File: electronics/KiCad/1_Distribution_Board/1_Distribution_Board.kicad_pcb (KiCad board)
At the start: 2 copper layers, 10 parts, among them J1 Conn_01x02, J2 Conn_01x04, J5 Conn_01x04, J6 Conn_01x10, J7 Conn_01x02, J8 Barrel_Jack, J9 Conn_01x02

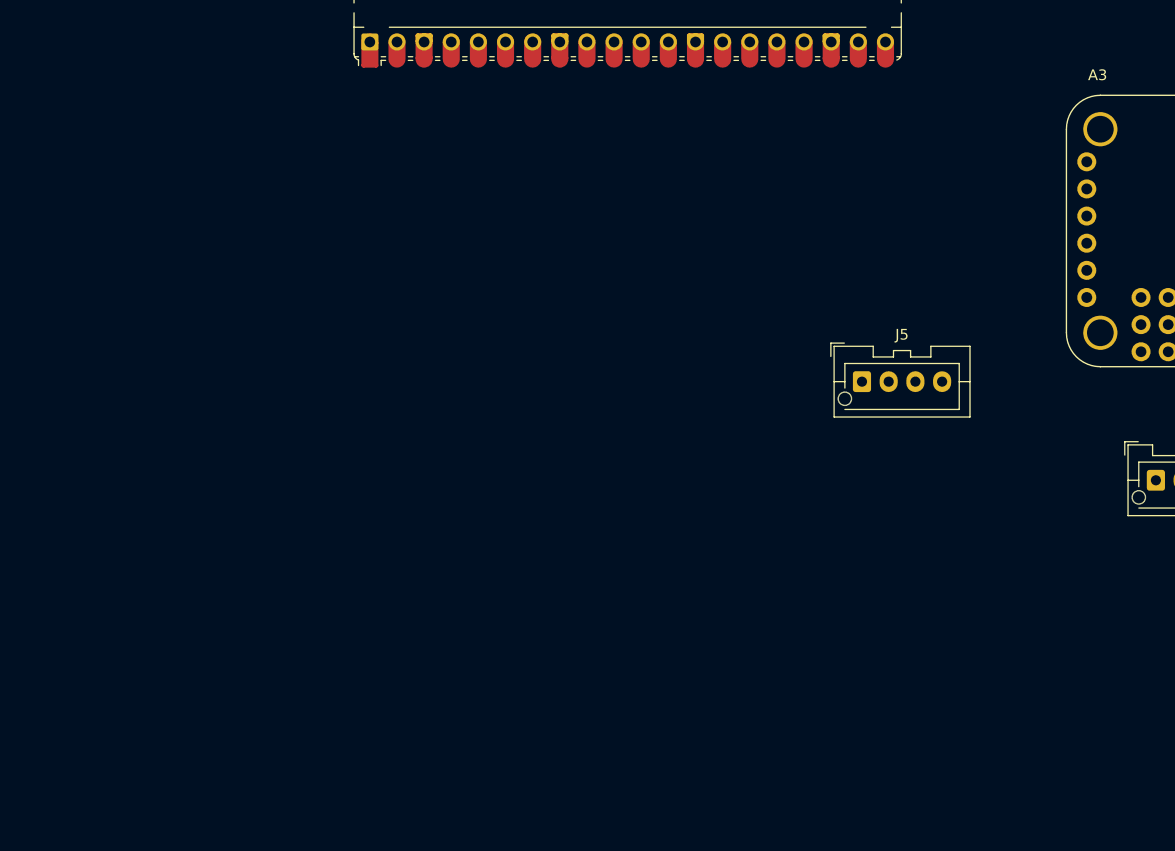
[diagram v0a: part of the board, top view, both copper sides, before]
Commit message: Updated schematics
Updated to remove additional stepper drive, corrected short on hall circuit. Removed level shifters for PWM signals.
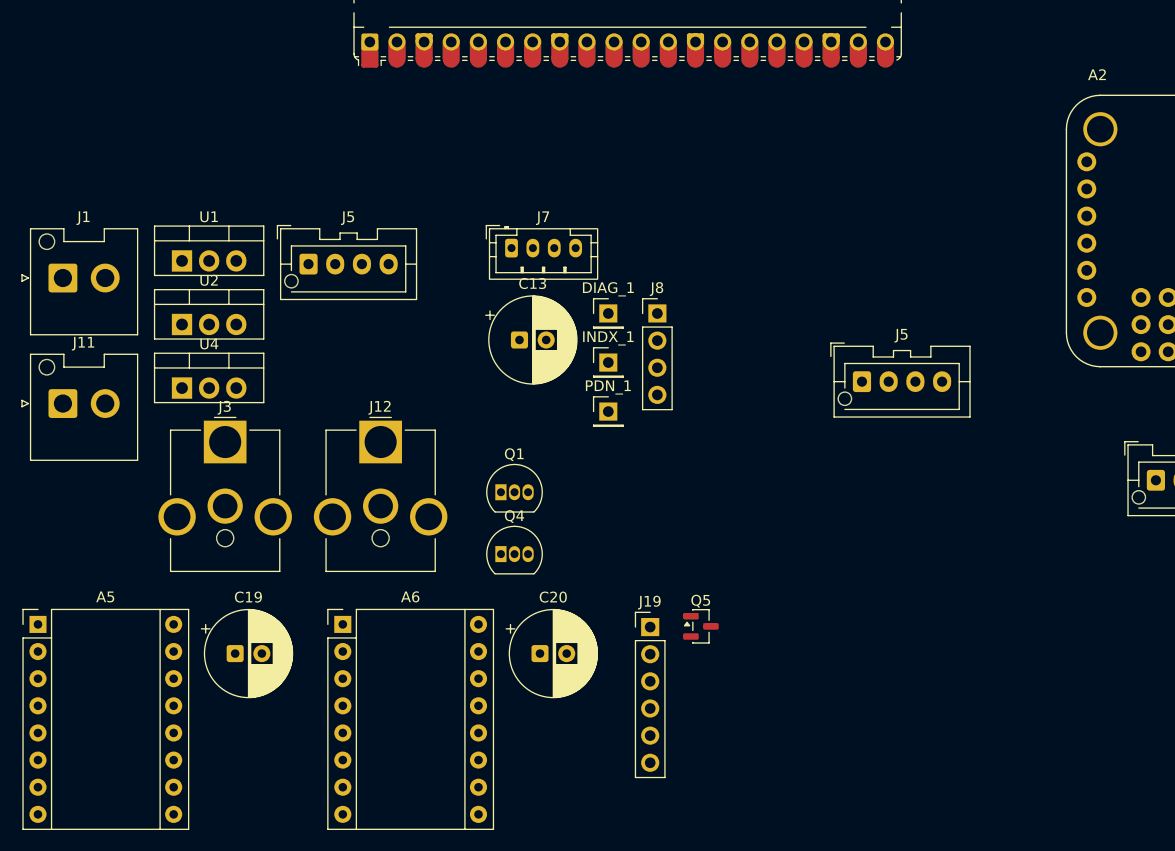
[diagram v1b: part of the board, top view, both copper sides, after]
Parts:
- added A5: Pololu_Breakout_TB6612FNG, Module:Pololu_Breakout-16_15.2x20.3mm, F.Cu at (37.7, 143.1)
- added A6: Pololu_Breakout_TB6612FNG, Module:Pololu_Breakout-16_15.2x20.3mm, F.Cu at (66.2, 143.1)
- added C13: 100uF, Capacitor_THT:CP_Radial_D8.0mm_P2.50mm, F.Cu at (82.8, 116.4)
- added C19: 100uF, Capacitor_THT:CP_Radial_D8.0mm_P2.50mm, F.Cu at (56.2, 145.8)
- added C20: 100uF, Capacitor_THT:CP_Radial_D8.0mm_P2.50mm, F.Cu at (84.7, 145.8)
- added DIAG_1: PTH, Connector_PinHeader_2.54mm:PinHeader_1x01_P2.54mm_Vertical, F.Cu at (91.1, 114.0)
- added INDX_1: PTH, Connector_PinHeader_2.54mm:PinHeader_1x01_P2.54mm_Vertical, F.Cu at (91.1, 118.5)
- added J1: JST VH, Connector_JST:JST_VH_B2P-VH-FB-B_1x02_P3.96mm_Vertical, F.Cu at (40.0, 110.6)
- added J11: JST VH, Connector_JST:JST_VH_B2P-VH-FB-B_1x02_P3.96mm_Vertical, F.Cu at (40.0, 122.4)
- added J12: Barrel_Jack, Connector_BarrelJack:BarrelJack_CUI_PJ-063AH_Horizontal_CircularHoles, F.Cu at (69.8, 126.0)
- added J19: Conn_01x06, Connector_PinHeader_2.54mm:PinHeader_1x06_P2.54mm_Vertical, F.Cu at (95.0, 143.3)
- added J3: Barrel_Jack, Connector_BarrelJack:BarrelJack_CUI_PJ-063AH_Horizontal_CircularHoles, F.Cu at (55.2, 126.0)
- added J5: Conn_01x04, Connector_JST:JST_XA_B04B-XASK-1-A_1x04_P2.50mm_Vertical, F.Cu at (63.0, 109.3)
- added J7: JST PH, Connector_JST:JST_PH_B4B-PH-K_1x04_P2.00mm_Vertical, F.Cu at (82.0, 107.8)
- added J8: Generic 2.54mm, Connector_PinHeader_2.54mm:PinHeader_1x04_P2.54mm_Vertical, F.Cu at (95.7, 114.0)
- added PDN_1: PTH, Connector_PinHeader_2.54mm:PinHeader_1x01_P2.54mm_Vertical, F.Cu at (91.1, 123.1)
- added Q1: TBD, Package_TO_SOT_THT:TO-92_Inline, F.Cu at (81.0, 130.7)
- added Q4: TBD, Package_TO_SOT_THT:TO-92_Inline, F.Cu at (81.0, 136.5)
- added Q5: DMG2305UX, Package_TO_SOT_SMD:SOT-23, F.Cu at (99.8, 143.2)
- added U1: LM7805_TO220, Package_TO_SOT_THT:TO-220-3_Vertical, F.Cu at (51.2, 109.0)
- added U2: LM317_TO-220, Package_TO_SOT_THT:TO-220-3_Vertical, F.Cu at (51.2, 115.0)
- added U4: LM7812_TO220, Package_TO_SOT_THT:TO-220-3_Vertical, F.Cu at (51.2, 120.9)
- renumbered A3 to A2
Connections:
- A1 pad 1: unconnected-(A1-GPIO0-Pad1) -> /UART0_TX
- A1 pad 11: unconnected-(A1-GPIO8-Pad11) -> /UART1_TX
- A1 pad 12: unconnected-(A1-GPIO9-Pad12) -> /UART1_RX
- A1 pad 2: unconnected-(A1-GPIO1-Pad2) -> /UART0_RX
- A1 pad 30: unconnected-(A1-RUN-Pad30) -> /~{RESET}
- A1 pad 39: unconnected-(A1-VSYS-Pad39) -> /VSYS
- A1 pad 40: unconnected-(A1-VBUS-Pad40) -> /VBUS
- A1 pad 6: unconnected-(A1-GPIO4-Pad6) -> /I2C0_SDA
- A1 pad 7: unconnected-(A1-GPIO5-Pad7) -> /I2C0_SCL
- A2 pad 10: unconnected-(A3-PWM_10-Pad10) -> Net-(A2-PWM_10)
- A2 pad 11: unconnected-(A3-PWM_11-Pad11) -> Net-(A2-PWM_11)
- A2 pad 12: unconnected-(A3-PWM_12-Pad12) -> Net-(A2-PWM_12)
- A2 pad 13: unconnected-(A3-PWM_13-Pad13) -> Net-(A2-PWM_13)
- A2 pad 14: unconnected-(A3-PWM_14-Pad14) -> Net-(A2-PWM_14)
- A2 pad 15: unconnected-(A3-PWM_15-Pad15) -> Net-(A2-PWM_15)
- A2 pad OE_1: /~{OE} -> unconnected-(A2-~{OE}-PadOE_1)_1
- A2 pad OE_2: /~{OE} -> unconnected-(A2-~{OE}-PadOE_1)
- A2 pad SCL_1: /SCL -> /I2C0_SCL
- A2 pad SCL_2: /SCL -> /I2C0_SCL
- A2 pad SDA_1: /SDA -> /I2C0_SDA
- A2 pad SDA_2: /SDA -> /I2C0_SDA

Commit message: footprint additions
Added Footprints to resistors and most components.
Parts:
- moved J12 211.4 mm to (268.0, 52.5)
- moved J5 205.5 mm to (254.1, 33.5)
- moved Q1 168.6 mm to (246.2, 97.0)
- moved Q4 168.6 mm to (246.2, 102.8)
- moved A5 166.3 mm to (186.7, 69.0)
- moved J2 162.1 mm to (116.5, 37.9)
- moved A6 154.3 mm to (185.4, 45.0)
- moved J7 139.9 mm to (219.7, 82.7)
- moved C19 132.8 mm to (164.8, 69.4)
- moved J19 132.6 mm to (226.8, 128.2)
- moved J8 131.9 mm to (217.6, 63.5)
- moved A2 104.6 mm to (143.9, 37.9)
- moved DIAG_1 104.1 mm to (168.2, 44.0)
- moved INDX_1 104.1 mm to (168.2, 48.6)
- moved PDN_1 104.1 mm to (168.2, 53.2)
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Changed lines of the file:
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@@
 	(footprint "Capacitor_THT:CP_Radial_D8.0mm_P2.50mm"
 		(layer "F.Cu")
-		(at 56.154698 145.78)
+		(at 164.79 69.41)
 		(descr "CP, Radial series, Radial, pin pitch=2.50mm, diameter=8mm, height=10mm, Electrolytic Capacitor")
 		(tags "CP Radial series Radial pin pitch 2.50mm diameter 8mm height 10mm Electrolytic Capacitor")
@@
 	(footprint "Connector_PinHeader_2.54mm:PinHeader_1x01_P2.54mm_Vertical"
 		(layer "F.Cu")
-		(at 91.08 113.95)
+		(at 168.16 44)
 		(descr "Through hole straight pin header, 1x01, 2.54mm pitch, single row")
 		(tags "Through hole pin header THT 1x01 2.54mm single row")
@@
 	(footprint "Connector_BarrelJack:BarrelJack_CUI_PJ-063AH_Horizontal_CircularHoles"
 		(layer "F.Cu")
-		(at 55.22 125.98)
+		(at 36.605 33.27)
 		(descr "Barrel Jack, 2.0mm ID, 5.5mm OD, 24V, 8A, no switch, https://www.cui.com/product/resource/pj-063ah.pdf")
 		(tags "barrel jack cui dc power")
@@
 	(footprint "Connector_JST:JST_XA_B10B-XASK-1-A_1x10_P2.50mm_Vertical"
 		(layer "F.Cu")
-		(at 142.33 129.56)
+		(at 157.42 144.647)
 		(descr "JST XA series connector, B10B-XASK-1-A (https://www.jst.com/wp-content/uploads/2021/01/eXA1.pdf), generated with kicad-footprint-generator")
 		(tags "connector JST XA vertical boss")
@@
 	(footprint "Module:Pololu_Breakout-16_15.2x20.3mm"
 		(layer "F.Cu")
-		(at 37.7 143.05)
+		(at 186.67 69.05)
 		(descr "Pololu Breakout 16-pin 15.2x20.3mm 0.6x0.8")
 		(tags "Pololu Breakout")
@@
 	(footprint "815:MODULE_815"
 		(layer "F.Cu")
-		(at 165.07 106.23)
+		(at 180.16 121.317)
 		(property "Reference" "A2"
 			(at -28.19 -14.585 0)
@@
 	(footprint "Package_TO_SOT_THT:TO-92_Inline"
 		(layer "F.Cu")
-		(at 81.03 136.47)
+		(at 246.25 102.83)
 		(descr "TO-92 leads in-line, narrow, oval pads, drill 0.75mm (see NXP sot054_po.pdf)")
 		(tags "to-92 sc-43 sc-43a sot54 PA33 transistor")
@@
 	(footprint "Connector_PinHeader_2.54mm:PinHeader_1x01_P2.54mm_Vertical"
 		(layer "F.Cu")
-		(at 91.08 123.13)
+		(at 168.16 53.18)
 		(descr "Through hole straight pin header, 1x01, 2.54mm pitch, single row")
 		(tags "Through hole pin header THT 1x01 2.54mm single row")
@@
 	(footprint "Connector_BarrelJack:BarrelJack_CUI_PJ-063AH_Horizontal_CircularHoles"
 		(layer "F.Cu")
-		(at 69.77 125.98)
+		(at 267.98 52.49)
 		(descr "Barrel Jack, 2.0mm ID, 5.5mm OD, 24V, 8A, no switch, https://www.cui.com/product/resource/pj-063ah.pdf")
 		(tags "barrel jack cui dc power")
@@
 	(footprint "Connector_PinHeader_2.54mm:PinHeader_1x01_P2.54mm_Vertical"
 		(layer "F.Cu")
-		(at 91.08 118.54)
+		(at 168.16 48.59)
 		(descr "Through hole straight pin header, 1x01, 2.54mm pitch, single row")
 		(tags "Through hole pin header THT 1x01 2.54mm single row")
@@
 	(footprint "Connector_JST:JST_PH_B4B-PH-K_1x04_P2.00mm_Vertical"
 		(layer "F.Cu")
-		(at 82.02 107.83)
+		(at 219.66 82.72)
 		(descr "JST PH series connector, B4B-PH-K (http://www.jst-mfg.com/product/pdf/eng/ePH.pdf), generated with kicad-footprint-generator")
 		(tags "connector JST PH vertical")
@@
 	(footprint "Connector_JST:JST_PH_B4B-PH-K_1x04_P2.00mm_Vertical"
 		(layer "F.Cu")
-		(at 257.78 117.39)
+		(at 116.46 37.94)
 		(descr "JST PH series connector, B4B-PH-K (http://www.jst-mfg.com/product/pdf/eng/ePH.pdf), generated with kicad-footprint-generator")
 		(tags "connector JST PH vertical")
@@
 	(footprint "Module:Pololu_Breakout-16_15.2x20.3mm"
 		(layer "F.Cu")
-		(at 66.23 143.05)
+		(at 185.43 45.03)
 		(descr "Pololu Breakout 16-pin 15.2x20.3mm 0.6x0.8")
 		(tags "Pololu Breakout")
@@
 	(footprint "Connector_PinHeader_2.54mm:PinHeader_1x02_P2.54mm_Vertical"
 		(layer "F.Cu")
-		(at 173.8 26.03)
+		(at 226.27 29.075)
 		(descr "Through hole straight pin header, 1x02, 2.54mm pitch, single row")
 		(tags "Through hole pin header THT 1x02 2.54mm single row")
@@
 	(footprint "Package_TO_SOT_THT:TO-92_Inline"
 		(layer "F.Cu")
-		(at 81.03 130.68)
+		(at 246.25 97.04)
 		(descr "TO-92 leads in-line, narrow, oval pads, drill 0.75mm (see NXP sot054_po.pdf)")
 		(tags "to-92 sc-43 sc-43a sot54 PA33 transistor")
@@
 	(footprint "TMC2209_SILENTSTEPSTICK:MODULE_TMC2209_SILENTSTEPSTICK"
 		(layer "F.Cu")
-		(at 232.63 93.37)
+		(at 143.93 37.94)
 		(property "Reference" "A2"
 			(at -5.075 -11.155 0)
@@
 	(footprint "Capacitor_THT:CP_Radial_D8.0mm_P2.50mm"
 		(layer "F.Cu")
-		(at 84.684698 145.78)
+		(at 165.19 86.64)
 		(descr "CP, Radial series, Radial, pin pitch=2.50mm, diameter=8mm, height=10mm, Electrolytic Capacitor")
 		(tags "CP Radial series Radial pin pitch 2.50mm diameter 8mm height 10mm Electrolytic Capacitor")
@@
 	(footprint "Package_TO_SOT_SMD:SOT-23"
 		(layer "F.Cu")
-		(at 99.75 143.23)
+		(at 68.0775 59.39)
 		(descr "SOT, 3 Pin (JEDEC TO-236 Var AB https://www.jedec.org/document_search?search_api_views_fulltext=TO-236), generated with kicad-footprint-generator ipc_gullwing_generator.py")
 		(tags "SOT TO_SOT_SMD")
@@
 	(footprint "Connector_PinHeader_2.54mm:PinHeader_1x06_P2.54mm_Vertical"
 		(layer "F.Cu")
-		(at 95 143.3)
+		(at 226.77 128.22)
 		(descr "Through hole straight pin header, 1x06, 2.54mm pitch, single row")
 		(tags "Through hole pin header THT 1x06 2.54mm single row")
@@
 	(footprint "Connector_JST:JST_XA_B04B-XASK-1-A_1x04_P2.50mm_Vertical"
 		(layer "F.Cu")
-		(at 114.82 120.33)
+		(at 194.78 142.337)
 		(descr "JST XA series connector, B04B-XASK-1-A (https://www.jst.com/wp-content/uploads/2021/01/eXA1.pdf), generated with kicad-footprint-generator")
 		(tags "connector JST XA vertical boss")
@@
 		)
 		(property "Value" "Conn_01x04"
-			(at 3.75 4.4 0)
+			(at 3.75 3.7 0)
 			(layer "F.Fab")
 			(effects
@@
 	(footprint "Connector_JST:JST_XA_B04B-XASK-1-A_1x04_P2.50mm_Vertical"
 		(layer "F.Cu")
-		(at 63.02 109.33)
+		(at 254.05 33.48)
 		(descr "JST XA series connector, B04B-XASK-1-A (https://www.jst.com/wp-content/uploads/2021/01/eXA1.pdf), generated with kicad-footprint-generator")
 		(tags "connector JST XA vertical boss")
@@
 		)
 		(property "Value" "Conn_01x04"
-			(at 3.75 4.4 0)
+			(at 3.75 3.7 0)
 			(layer "F.Fab")
 			(effects
@@
 	(footprint "Connector_PinHeader_2.54mm:PinHeader_1x02_P2.54mm_Vertical"
 		(layer "F.Cu")
-		(at 178.39 26.03)
+		(at 218.74 26.03)
 		(descr "Through hole straight pin header, 1x02, 2.54mm pitch, single row")
 		(tags "Through hole pin header THT 1x02 2.54mm single row")
@@
 	(footprint "Connector_PinHeader_2.54mm:PinHeader_1x04_P2.54mm_Vertical"
 		(layer "F.Cu")
-		(at 95.67 113.95)
+		(at 217.6 63.52)
 		(descr "Through hole straight pin header, 1x04, 2.54mm pitch, single row")
 		(tags "Through hole pin header THT 1x04 2.54mm single row")
@@
 		)
 		(property "Value" "Generic 2.54mm"
-			(at 0 10 0)
+			(at 1.77 0.88 0)
 			(layer "F.Fab")
 			(effects
@@
 	(footprint "Capacitor_THT:CP_Radial_D8.0mm_P2.50mm"
 		(layer "F.Cu")
-		(at 82.764698 116.43)
+		(at 140.24 62.29)
 		(descr "CP, Radial series, Radial, pin pitch=2.50mm, diameter=8mm, height=10mm, Electrolytic Capacitor")
 		(tags "CP Radial series Radial pin pitch 2.50mm diameter 8mm height 10mm Electrolytic Capacitor")

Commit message: Updated to add 2 more steppers
Updated to add two more steppers, dual with the motor controllers. they will be either or. Layout hole pattern started. Still need some footprints assigned.
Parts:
- removed J2: Conn_01x04, Connector_JST:JST_PH_B4B-PH-K_1x04_P2.00mm_Vertical
- removed J8: Barrel_Jack, Connector_BarrelJack:BarrelJack_CUI_PJ-063AH_Horizontal_CircularHoles
- removed J9: Conn_01x02, Connector_JST:JST_VH_B2P-VH-FB-B_1x02_P3.96mm_Vertical
- added A2: TMC2209_SILENTSTEPSTICK, TMC2209_SILENTSTEPSTICK:MODULE_TMC2209_SILENTSTEPSTICK, F.Cu at (483.6, 105.0)
- added A2: TMC2209_SILENTSTEPSTICK, TMC2209_SILENTSTEPSTICK:MODULE_TMC2209_SILENTSTEPSTICK, F.Cu at (483.6, 75.0)
- added C601: 0.1uf, Capacitor_SMD:C_0805_2012Metric_Pad1.18x1.45mm_HandSolder, F.Cu at (97.7, 152.5)
- added C602: 0.1uf, Capacitor_SMD:C_0805_2012Metric_Pad1.18x1.45mm_HandSolder, F.Cu at (97.7, 155.5)
- added C603: 0.1uf, Capacitor_SMD:C_0805_2012Metric_Pad1.18x1.45mm_HandSolder, F.Cu at (97.7, 158.5)
- added C604: 0.1uf, Capacitor_SMD:C_0805_2012Metric_Pad1.18x1.45mm_HandSolder, F.Cu at (97.7, 161.5)
- added C701: 100uF, Capacitor_THT:CP_Radial_D8.0mm_P2.50mm, F.Cu at (94.1, 124.1)
- added C801: 100uF, Capacitor_THT:CP_Radial_D8.0mm_P2.50mm, F.Cu at (117.4, 124.1)
- added DIAG_701: PTH, Connector_PinHeader_2.54mm:PinHeader_1x01_P2.54mm_Vertical, F.Cu at (88.1, 115.0)
- added DIAG_801: PTH, Connector_PinHeader_2.54mm:PinHeader_1x01_P2.54mm_Vertical, F.Cu at (111.4, 115.0)
- added F301: 1812L150/24MR, Fuse:Fuse_1812_4532Metric_Pad1.30x3.40mm_HandSolder, F.Cu at (114.3, 165.0)
- added F401: 1812L150/24MR, Fuse:Fuse_1812_4532Metric_Pad1.30x3.40mm_HandSolder, F.Cu at (114.3, 150.9)
- added INDX_701: PTH, Connector_PinHeader_2.54mm:PinHeader_1x01_P2.54mm_Vertical, F.Cu at (88.1, 119.6)
- added INDX_801: PTH, Connector_PinHeader_2.54mm:PinHeader_1x01_P2.54mm_Vertical, F.Cu at (111.4, 119.6)
- added J201: Jumper Pins, Connector_PinHeader_2.54mm:PinHeader_1x03_P2.54mm_Vertical, F.Cu at (136.4, 156.8)
- added J202: Jumper Pins, Connector_PinHeader_2.54mm:PinHeader_1x03_P2.54mm_Vertical, F.Cu at (141.0, 156.8)
- added J301: Conn_01x02, Connector_PinHeader_2.54mm:PinHeader_1x02_P2.54mm_Vertical, F.Cu at (112.9, 157.7)
- added J302: Conn_01x02, Connector_PinHeader_2.54mm:PinHeader_1x02_P2.54mm_Vertical, F.Cu at (117.5, 157.7)
- added J401: Conn_01x02, Connector_PinHeader_2.54mm:PinHeader_1x02_P2.54mm_Vertical, F.Cu at (112.9, 143.6)
- added J402: Conn_01x02, Connector_PinHeader_2.54mm:PinHeader_1x02_P2.54mm_Vertical, F.Cu at (117.5, 143.6)
- added J601: Generic 2.54mm, Connector_PinHeader_2.54mm:PinHeader_1x03_P2.54mm_Vertical, F.Cu at (162.9, 174.9)
- added J602: Generic 2.54mm, Connector_PinHeader_2.54mm:PinHeader_1x02_P2.54mm_Vertical, F.Cu at (101.7, 143.6)
- added J603: Generic 2.54mm, Connector_PinHeader_2.54mm:PinHeader_1x03_P2.54mm_Vertical, F.Cu at (153.7, 174.9)
- added J604: Generic 2.54mm, Connector_PinHeader_2.54mm:PinHeader_1x02_P2.54mm_Vertical, F.Cu at (106.3, 143.6)
- added J605: Generic 2.54mm, Connector_PinHeader_2.54mm:PinHeader_1x03_P2.54mm_Vertical, F.Cu at (158.3, 174.9)
- added J606: Generic 2.54mm, Connector_PinHeader_2.54mm:PinHeader_1x03_P2.54mm_Vertical, F.Cu at (167.5, 174.9)
- added J701: Jumper Pins, Connector_PinHeader_2.54mm:PinHeader_1x03_P2.54mm_Vertical, F.Cu at (147.6, 156.8)
- added J702: Jumper Pins, Connector_PinHeader_2.54mm:PinHeader_1x03_P2.54mm_Vertical, F.Cu at (161.5, 156.9)
- added J703: JST PH, Connector_JST:JST_PH_B4B-PH-K_1x04_P2.00mm_Vertical, F.Cu at (93.4, 115.5)
- added J704: Generic 2.54mm, Connector_PinHeader_2.54mm:PinHeader_1x04_P2.54mm_Vertical, F.Cu at (88.1, 128.8)
- added J801: Jumper Pins, Connector_PinHeader_2.54mm:PinHeader_1x03_P2.54mm_Vertical, F.Cu at (136.4, 168.4)
- added J802: Jumper Pins, Connector_PinHeader_2.54mm:PinHeader_1x03_P2.54mm_Vertical, F.Cu at (141.0, 168.4)
- added J803: JST PH, Connector_JST:JST_PH_B4B-PH-K_1x04_P2.00mm_Vertical, F.Cu at (116.7, 115.5)
- added J804: Generic 2.54mm, Connector_PinHeader_2.54mm:PinHeader_1x04_P2.54mm_Vertical, F.Cu at (111.4, 128.8)
- added PDN_701: PTH, Connector_PinHeader_2.54mm:PinHeader_1x01_P2.54mm_Vertical, F.Cu at (88.1, 124.2)
- added PDN_801: PTH, Connector_PinHeader_2.54mm:PinHeader_1x01_P2.54mm_Vertical, F.Cu at (111.4, 124.2)
- added R101: 10k, Resistor_SMD:R_0805_2012Metric_Pad1.20x1.40mm_HandSolder, F.Cu at (76.7, 148.7)
- added R102: 10k, Resistor_SMD:R_0805_2012Metric_Pad1.20x1.40mm_HandSolder, F.Cu at (76.7, 142.8)
- added R103: 10k, Resistor_SMD:R_0805_2012Metric_Pad1.20x1.40mm_HandSolder, F.Cu at (76.7, 145.7)
- added R201: 10k, Resistor_SMD:R_0805_2012Metric_Pad1.20x1.40mm_HandSolder, F.Cu at (76.7, 114.2)
- added R202: 10k, Resistor_SMD:R_0805_2012Metric_Pad1.20x1.40mm_HandSolder, F.Cu at (76.7, 117.2)
- added R203: 10k, Resistor_SMD:R_0805_2012Metric_Pad1.20x1.40mm_HandSolder, F.Cu at (76.7, 126.0)
- added R204: 10k, Resistor_SMD:R_0805_2012Metric_Pad1.20x1.40mm_HandSolder, F.Cu at (76.7, 120.1)
- added R205: 10k, Resistor_SMD:R_0805_2012Metric_Pad1.20x1.40mm_HandSolder, F.Cu at (76.7, 129.0)
- added R206: 10k, Resistor_SMD:R_0805_2012Metric_Pad1.20x1.40mm_HandSolder, F.Cu at (76.7, 134.9)
- added R207: 10k, Resistor_SMD:R_0805_2012Metric_Pad1.20x1.40mm_HandSolder, F.Cu at (76.7, 137.8)
- added R208: 10k, Resistor_SMD:R_0805_2012Metric_Pad1.20x1.40mm_HandSolder, F.Cu at (76.7, 131.9)
- added R209: 10k, Resistor_SMD:R_0805_2012Metric_Pad1.20x1.40mm_HandSolder, F.Cu at (76.7, 123.1)
- added R601: 10K, Resistor_SMD:R_0805_2012Metric_Pad1.20x1.40mm_HandSolder, F.Cu at (88.2, 152.4)
- added R602: 100, Resistor_SMD:R_0805_2012Metric_Pad1.20x1.40mm_HandSolder, F.Cu at (88.2, 155.4)
- added R603: 150, Resistor_SMD:R_0805_2012Metric_Pad1.20x1.40mm_HandSolder, F.Cu at (83.5, 152.4)
- added R604: 10k, Resistor_SMD:R_0805_2012Metric_Pad1.20x1.40mm_HandSolder, F.Cu at (83.5, 155.4)
- added R605: 10K, Resistor_SMD:R_0805_2012Metric_Pad1.20x1.40mm_HandSolder, F.Cu at (88.2, 158.3)
- added R606: 100, Resistor_SMD:R_0805_2012Metric_Pad1.20x1.40mm_HandSolder, F.Cu at (88.2, 161.3)
- added R607: 150, Resistor_SMD:R_0805_2012Metric_Pad1.20x1.40mm_HandSolder, F.Cu at (83.5, 158.3)
- added R608: 10k, Resistor_SMD:R_0805_2012Metric_Pad1.20x1.40mm_HandSolder, F.Cu at (83.5, 161.3)
- added R609: 10K, Resistor_SMD:R_0805_2012Metric_Pad1.20x1.40mm_HandSolder, F.Cu at (93.0, 152.4)
- added R610: 100, Resistor_SMD:R_0805_2012Metric_Pad1.20x1.40mm_HandSolder, F.Cu at (93.0, 155.4)
- added R611: 10K, Resistor_SMD:R_0805_2012Metric_Pad1.20x1.40mm_HandSolder, F.Cu at (93.0, 158.3)
- added R612: 100, Resistor_SMD:R_0805_2012Metric_Pad1.20x1.40mm_HandSolder, F.Cu at (93.0, 161.3)
- added R701: 10k, Resistor_SMD:R_0805_2012Metric_Pad1.20x1.40mm_HandSolder, F.Cu at (83.5, 114.2)
- added R702: 10k, Resistor_SMD:R_0805_2012Metric_Pad1.20x1.40mm_HandSolder, F.Cu at (83.5, 117.2)
- added R703: 10k, Resistor_SMD:R_0805_2012Metric_Pad1.20x1.40mm_HandSolder, F.Cu at (83.5, 120.1)
- added R704: 10k, Resistor_SMD:R_0805_2012Metric_Pad1.20x1.40mm_HandSolder, F.Cu at (83.5, 123.1)
- added R705: 10k, Resistor_SMD:R_0805_2012Metric_Pad1.20x1.40mm_HandSolder, F.Cu at (83.5, 126.0)
- added R706: 10k, Resistor_SMD:R_0805_2012Metric_Pad1.20x1.40mm_HandSolder, F.Cu at (83.5, 129.0)
- added R707: 10k, Resistor_SMD:R_0805_2012Metric_Pad1.20x1.40mm_HandSolder, F.Cu at (83.5, 131.9)
- added R708: 10k, Resistor_SMD:R_0805_2012Metric_Pad1.20x1.40mm_HandSolder, F.Cu at (83.5, 134.9)
- added R709: 10k, Resistor_SMD:R_0805_2012Metric_Pad1.20x1.40mm_HandSolder, F.Cu at (83.5, 137.8)
- added R801: 10k, Resistor_SMD:R_0805_2012Metric_Pad1.20x1.40mm_HandSolder, F.Cu at (106.7, 114.2)
- added R802: 10k, Resistor_SMD:R_0805_2012Metric_Pad1.20x1.40mm_HandSolder, F.Cu at (106.7, 117.2)
- added R803: 10k, Resistor_SMD:R_0805_2012Metric_Pad1.20x1.40mm_HandSolder, F.Cu at (106.7, 120.1)
- added R804: 10k, Resistor_SMD:R_0805_2012Metric_Pad1.20x1.40mm_HandSolder, F.Cu at (106.7, 123.1)
- added R805: 10k, Resistor_SMD:R_0805_2012Metric_Pad1.20x1.40mm_HandSolder, F.Cu at (106.7, 126.0)
- added R806: 10k, Resistor_SMD:R_0805_2012Metric_Pad1.20x1.40mm_HandSolder, F.Cu at (106.7, 129.0)
- added R807: 10k, Resistor_SMD:R_0805_2012Metric_Pad1.20x1.40mm_HandSolder, F.Cu at (106.7, 131.9)
- added R808: 10k, Resistor_SMD:R_0805_2012Metric_Pad1.20x1.40mm_HandSolder, F.Cu at (106.7, 134.9)
- added R809: 10k, Resistor_SMD:R_0805_2012Metric_Pad1.20x1.40mm_HandSolder, F.Cu at (106.7, 137.8)
- added REF**: MountingHole_3.2mm_M3_DIN965_Pad, MountingHole:MountingHole_3.2mm_M3_DIN965_Pad, F.Cu at (515.0, 95.0)
- added REF**: MountingHole_3.2mm_M3_DIN965_Pad, MountingHole:MountingHole_3.2mm_M3_DIN965_Pad, F.Cu at (335.0, 35.0)
- added REF**: MountingHole_3.2mm_M3_DIN965_Pad, MountingHole:MountingHole_3.2mm_M3_DIN965_Pad, F.Cu at (395.0, 95.0)
- added REF**: MountingHole_3.2mm_M3_DIN965_Pad, MountingHole:MountingHole_3.2mm_M3_DIN965_Pad, F.Cu at (395.0, 35.0)
- added REF**: MountingHole_3.2mm_M3_DIN965_Pad, MountingHole:MountingHole_3.2mm_M3_DIN965_Pad, F.Cu at (455.0, 35.0)
- added REF**: MountingHole_3.2mm_M3_DIN965_Pad, MountingHole:MountingHole_3.2mm_M3_DIN965_Pad, F.Cu at (455.0, 155.0)
- added REF**: MountingHole_3.2mm_M3_DIN965_Pad, MountingHole:MountingHole_3.2mm_M3_DIN965_Pad, F.Cu at (515.0, 155.0)
- added REF**: MountingHole_3.2mm_M3_DIN965_Pad, MountingHole:MountingHole_3.2mm_M3_DIN965_Pad, F.Cu at (335.0, 155.0)
- added REF**: MountingHole_3.2mm_M3_DIN965_Pad, MountingHole:MountingHole_3.2mm_M3_DIN965_Pad, F.Cu at (455.0, 95.0)
- added REF**: MountingHole_3.2mm_M3_DIN965_Pad, MountingHole:MountingHole_3.2mm_M3_DIN965_Pad, F.Cu at (335.0, 95.0)
- added REF**: MountingHole_3.2mm_M3_DIN965_Pad, MountingHole:MountingHole_3.2mm_M3_DIN965_Pad, F.Cu at (395.0, 155.0)
- added REF**: MountingHole_3.2mm_M3_DIN965_Pad, MountingHole:MountingHole_3.2mm_M3_DIN965_Pad, F.Cu at (515.0, 35.0)
- moved A2 339.8 mm to (483.6, 46.2)
- moved A101 332.0 mm to (423.9, 53.7), turned to 0 degrees
- moved A301 271.0 mm to (448.9, 108.7), turned to -90 degrees
- moved A401 235.6 mm to (418.9, 108.7), turned to -90 degrees
- moved J101 209.8 mm to (342.0, 45.0), turned to -90 degrees
- moved A102 193.3 mm to (366.2, 68.8), turned to -90 degrees
- moved J102 126.5 mm to (343.0, 78.3)
- moved U503 79.0 mm to (67.2, 43.5)
- moved J501 79.0 mm to (56.0, 33.2)
- moved J502 79.0 mm to (56.0, 45.0)
- moved U501 79.0 mm to (67.2, 31.6)
- moved U502 79.0 mm to (67.2, 37.6)
- renumbered A1 to A101, A2 to A102, A6 to A301, A5 to A401, C13 to C201, C20 to C301, C19 to C401, DIAG_1 to DIAG_201, INDX_1 to INDX_201, J6 to J101, J19 to J102, J7 to J203, J8 to J204, J1 to J501, J11 to J502, J12 to J503, J3 to J504, J5 to J505, PDN_1 to PDN_201, Q5 to Q101, Q1 to Q601, Q4 to Q602, U1 to U501, U2 to U502, U4 to U503

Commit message: Separated layout components
Moved components into separate zones for layout. Picked PCB size with the spacing designed in.
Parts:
- removed J1, J7: Conn_01x02, Connector_PinHeader_2.54mm:PinHeader_1x02_P2.54mm_Vertical
- moved A2 359.2 mm to (125.0, 85.0), turned to -90 degrees
- moved A2 358.8 mm to (125.0, 65.0), turned to -90 degrees
- moved A2 358.7 mm to (125.0, 45.0), turned to -90 degrees
- moved A301 355.8 mm to (93.2, 115.4)
- moved A101 333.9 mm to (90.0, 50.0)
- moved A102 306.3 mm to (60.0, 60.0)
- moved J101 305.0 mm to (37.0, 40.0)
- moved J102 305.0 mm to (38.0, 73.3)
- moved REF** 305.0 mm to (210.0, 90.0)
- moved REF** 305.0 mm to (30.0, 30.0)
- moved REF** 305.0 mm to (90.0, 90.0)
- moved REF** 305.0 mm to (90.0, 30.0)
- moved REF** 305.0 mm to (150.0, 30.0)
- moved REF** 305.0 mm to (150.0, 150.0)
- moved REF** 305.0 mm to (210.0, 150.0)
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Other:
- board outline added: 130 x 130 mm
